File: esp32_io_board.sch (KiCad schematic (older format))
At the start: 58 parts, among them J1 USB_B_Micro, J11 Conn_01x02, J12 Conn_01x02, J13 Conn_01x02, J14 Conn_01x02, J2 Conn_02x04_Counter_Clockwise, J3 Conn_01x02, J4 Conn_01x04, J5 RASPBERRYPI-40-PIN-GPIO, J7 Conn_01x02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

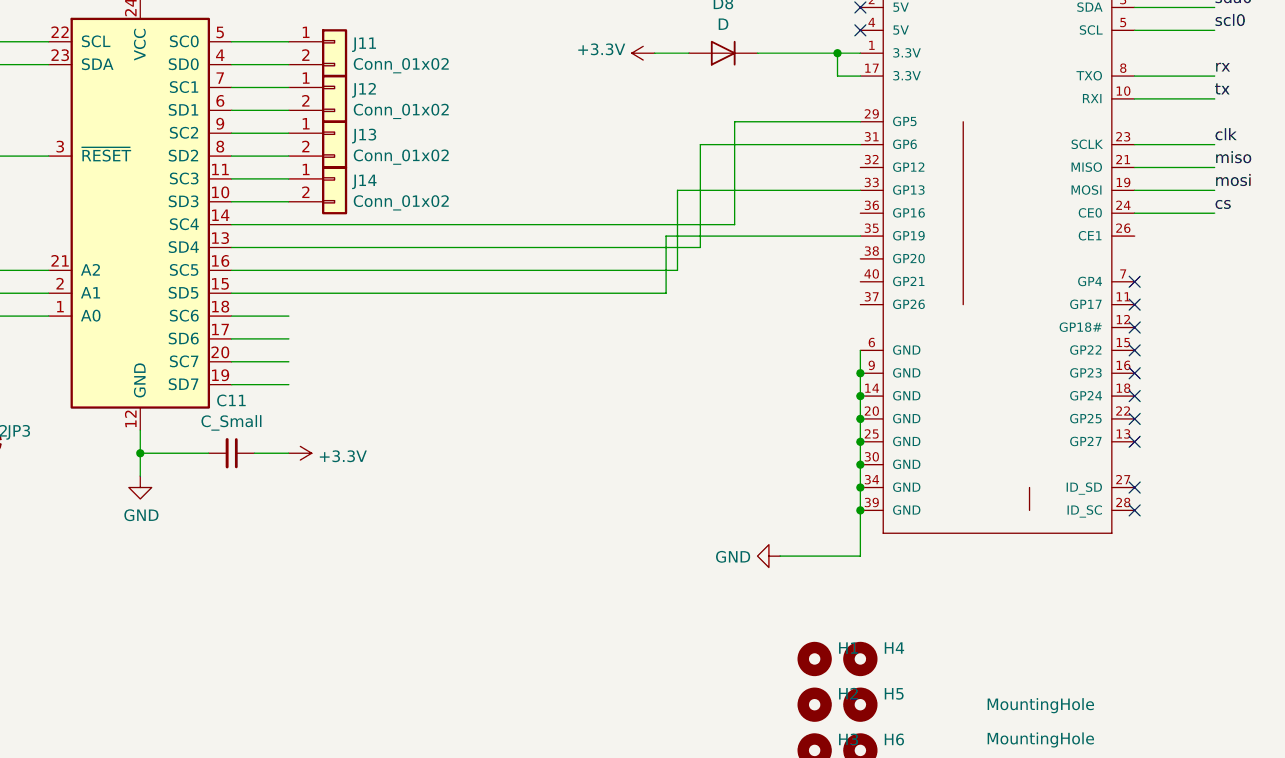
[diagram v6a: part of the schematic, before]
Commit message: raspberry pi integration
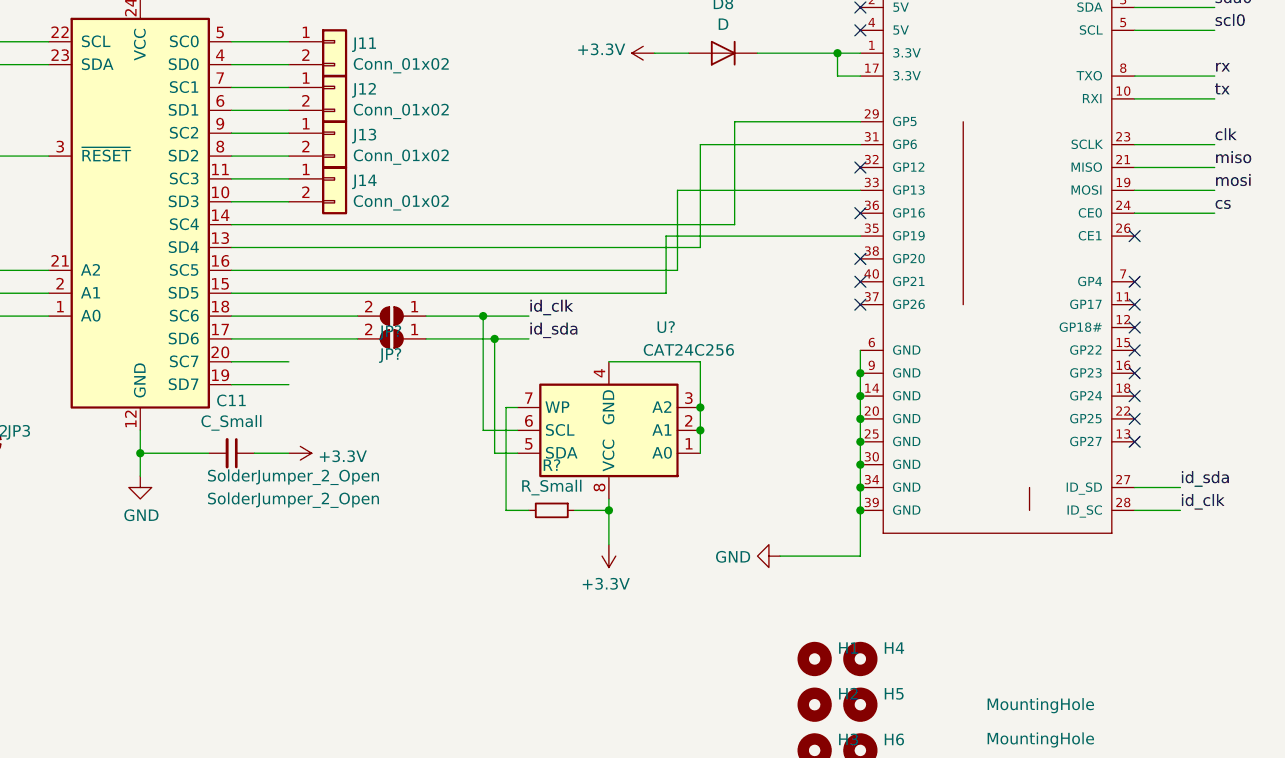
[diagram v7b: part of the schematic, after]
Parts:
- added JP? (x2): SolderJumper_2_Open, Jumper:SolderJumper-2_P1.3mm_Open_RoundedPad1.0x1.5mm, symbol Jumper:SolderJumper_2_Open
- added R?: R_Small, symbol Device:R_Small
- added U?: CAT24C256, symbol Memory_EEPROM:CAT24C256
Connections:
- net +3V3: now also R?.1, U?.8 (VCC)
- net id_sda: now reaches J5.27 (ID_SD)
- net id_sda: now also JP?.1 (A), U?.5 (SDA)
- net id_clk: now reaches J5.28 (ID_SC)
- net id_clk: now also JP?.1 (A), U?.6 (SCL)
- net at U6.17 (SD6): now also JP?.2 (B)
- net at U6.18 (SC6): now also JP?.2 (B)
- new net: U?.1 (A0), U?.2 (A1), U?.3 (A2), U?.4 (GND)
- new net: R?.2, U?.7 (WP)
- no-connect marks 30 -> 34
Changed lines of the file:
@@
 	12300 8450 12550 8450
-Wire Wire Line
-	12300 8950 12550 8950
-Wire Wire Line
-	12300 9050 12550 9050
 Wire Wire Line
 	12300 9150 12550 9150
@@
 NoConn ~ 16250 9400
 NoConn ~ 16250 9500
-NoConn ~ 16250 9700
-NoConn ~ 16250 9800
 NoConn ~ 9950 6950
 NoConn ~ 10250 6950
@@
 Wire Wire Line
 	14200 8600 14200 8850
+$Comp
+L Memory_EEPROM:CAT24C256 U?
+U 1 1 5C224C63
+P 13950 9450
+F 0 "U?" H 13700 9000 50  0000 C CNN
+F 1 "CAT24C256" H 13600 9100 50  0000 C CNN
+F 2 "" H 13950 9450 50  0001 C CNN
+F 3 "https://www.onsemi.cn/PowerSolutions/document/CAT24C256-D.PDF" H 13950 9450 50  0001 C CNN
+	1    13950 9450
+	-1   0    0    1
+$EndComp
+Wire Wire Line
+	13550 9450 13400 9450
+Wire Wire Line
+	13400 9450 13400 8950
+Wire Wire Line
+	12300 8950 12850 8950
+Wire Wire Line
+	13450 9050 13450 9550
+Wire Wire Line
+	13450 9550 13550 9550
+Wire Wire Line
+	12300 9050 12850 9050
+Wire Wire Line
+	14350 9550 14350 9450
+Wire Wire Line
+	14350 9150 13950 9150
+Connection ~ 14350 9350
+Wire Wire Line
+	14350 9350 14350 9150
+Connection ~ 14350 9450
+Wire Wire Line
+	14350 9450 14350 9350
+Wire Wire Line
+	13950 9750 13950 9800
+$Comp
+L power:+3.3V #PWR?
+U 1 1 5C2F17EF
+P 13950 9950
+F 0 "#PWR?" H 13950 9800 50  0001 C CNN
+F 1 "+3.3V" H 13965 10123 50  0000 C CNN
+F 2 "" H 13950 9950 50  0001 C CNN
+F 3 "" H 13950 9950 50  0001 C CNN
+	1    13950 9950
+	-1   0    0    1
+$EndComp
+Connection ~ 13450 9050
+Wire Wire Line
+	13400 8950 13600 8950
+Connection ~ 13400 8950
+Wire Wire Line
+	13450 9050 13600 9050
+Text Label 13600 8950 0    50   ~ 0
+id_clk
+Text Label 13600 9050 0    50   ~ 0
+id_sda
+Wire Wire Line
+	16250 9700 16450 9700
+Wire Wire Line
+	16250 9800 16450 9800
+Text Label 16450 9800 0    50   ~ 0
+id_clk
+Text Label 16450 9700 0    50   ~ 0
+id_sda
+$Comp
+L Jumper:SolderJumper_2_Open JP?
+U 1 1 5C387087
+P 13000 8950
+F 0 "JP?" H 12954 9018 50  0000 L CNN
+F 1 "SolderJumper_2_Open" H 13050 9650 50  0000 L CNN
+F 2 "Jumper:SolderJumper-2_P1.3mm_Open_RoundedPad1.0x1.5mm" H 13000 8950 50  0001 C CNN
+F 3 "~" H 13000 8950 50  0001 C CNN
+	1    13000 8950
+	-1   0    0    1
+$EndComp
+Wire Wire Line
+	13150 8950 13400 8950
+Wire Wire Line
+	13150 9050 13450 9050
+$Comp
+L Jumper:SolderJumper_2_Open JP?
+U 1 1 5C3A9876
+P 13000 9050
+F 0 "JP?" H 12954 9118 50  0000 L CNN
+F 1 "SolderJumper_2_Open" H 13050 9750 50  0000 L CNN
+F 2 "Jumper:SolderJumper-2_P1.3mm_Open_RoundedPad1.0x1.5mm" H 13000 9050 50  0001 C CNN
+F 3 "~" H 13000 9050 50  0001 C CNN
+	1    13000 9050
+	-1   0    0    1
+$EndComp
+NoConn ~ 15050 8300
+NoConn ~ 15050 8500
+NoConn ~ 15050 8700
+NoConn ~ 15050 8800
+NoConn ~ 15050 8900
+NoConn ~ 16250 8600
+Wire Wire Line
+	13550 9350 13500 9350
+Wire Wire Line
+	13500 9350 13500 9800
+$Comp
+L Device:R_Small R?
+U 1 1 5C4EC3FB
+P 13700 9800
+F 0 "R?" V 13504 9800 50  0000 C CNN
+F 1 "R_Small" V 13595 9800 50  0000 C CNN
+F 2 "" H 13700 9800 50  0001 C CNN
+F 3 "~" H 13700 9800 50  0001 C CNN
+	1    13700 9800
+	0    1    1    0
+$EndComp
+Wire Wire Line
+	13500 9800 13600 9800
+Wire Wire Line
+	13800 9800 13950 9800
+Connection ~ 13950 9800
+Wire Wire Line
+	13950 9800 13950 9950
 $EndSCHEMATC

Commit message: i2c jumpers
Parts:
- added JP? (x4): SolderJumper_2_Open, Jumper:SolderJumper-2_P1.3mm_Open_RoundedPad1.0x1.5mm, symbol Jumper:SolderJumper_2_Open
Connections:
- net at J5.29 (GP5): now also JP?.1 (A); no longer U6.14 (SC4)
- net at J5.31 (GP6): now also JP?.1 (A); no longer U6.13 (SD4)
- net at J5.33 (GP13): now also JP?.1 (A); no longer U6.16 (SC5)
- net at J5.35 (GP19): now also JP?.1 (A); no longer U6.15 (SD5)
- new net: JP?.2 (B), U6.15 (SD5)
- new net: JP?.2 (B), U6.16 (SC5)
- new net: JP?.2 (B), U6.13 (SD4)
- new net: JP?.2 (B), U6.14 (SC4)
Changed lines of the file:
@@
 	14500 8100 15050 8100
 Wire Wire Line
-	12300 8550 14500 8550
+	12300 8550 12850 8550
 Wire Wire Line
 	14350 8650 14350 8200
@@
 	14350 8200 15050 8200
 Wire Wire Line
-	12300 8650 14350 8650
+	12300 8650 12850 8650
 Wire Wire Line
 	14250 8750 14250 8400
 Wire Wire Line
-	12300 8750 14250 8750
+	12300 8750 12850 8750
 Wire Wire Line
 	14250 8400 15050 8400
 Wire Wire Line
-	12300 8850 14200 8850
+	12300 8850 12850 8850
 Wire Wire Line
 	14200 8600 15050 8600
@@
 P 13000 8950
 F 0 "JP?" H 12954 9018 50  0000 L CNN
-F 1 "SolderJumper_2_Open" H 13050 9650 50  0000 L CNN
+F 1 "SolderJumper_2_Open" H 12950 10000 50  0000 L CNN
 F 2 "Jumper:SolderJumper-2_P1.3mm_Open_RoundedPad1.0x1.5mm" H 13000 8950 50  0001 C CNN
 F 3 "~" H 13000 8950 50  0001 C CNN
@@
 P 13000 9050
 F 0 "JP?" H 12954 9118 50  0000 L CNN
-F 1 "SolderJumper_2_Open" H 13050 9750 50  0000 L CNN
+F 1 "SolderJumper_2_Open" H 12950 10100 50  0000 L CNN
 F 2 "Jumper:SolderJumper-2_P1.3mm_Open_RoundedPad1.0x1.5mm" H 13000 9050 50  0001 C CNN
 F 3 "~" H 13000 9050 50  0001 C CNN
@@
 Wire Wire Line
 	13950 9800 13950 9950
+Wire Wire Line
+	13150 8850 14200 8850
+Wire Wire Line
+	13150 8750 14250 8750
+Wire Wire Line
+	13150 8650 14350 8650
+Wire Wire Line
+	13150 8550 14500 8550
+$Comp
+L Jumper:SolderJumper_2_Open JP?
+U 1 1 5C239362
+P 13000 8850
+F 0 "JP?" H 12954 8918 50  0000 L CNN
+F 1 "SolderJumper_2_Open" H 12950 10200 50  0000 L CNN
+F 2 "Jumper:SolderJumper-2_P1.3mm_Open_RoundedPad1.0x1.5mm" H 13000 8850 50  0001 C CNN
+F 3 "~" H 13000 8850 50  0001 C CNN
+	1    13000 8850
+	-1   0    0    1
+$EndComp
+$Comp
+L Jumper:SolderJumper_2_Open JP?
+U 1 1 5C2397B0
+P 13000 8750
+F 0 "JP?" H 12954 8818 50  0000 L CNN
+F 1 "SolderJumper_2_Open" H 12950 10500 50  0000 L CNN
+F 2 "Jumper:SolderJumper-2_P1.3mm_Open_RoundedPad1.0x1.5mm" H 13000 8750 50  0001 C CNN
+F 3 "~" H 13000 8750 50  0001 C CNN
+	1    13000 8750
+	-1   0    0    1
+$EndComp
+$Comp
+L Jumper:SolderJumper_2_Open JP?
+U 1 1 5C239840
+P 13000 8650
+F 0 "JP?" H 12954 8718 50  0000 L CNN
+F 1 "SolderJumper_2_Open" H 12950 10400 50  0000 L CNN
+F 2 "Jumper:SolderJumper-2_P1.3mm_Open_RoundedPad1.0x1.5mm" H 13000 8650 50  0001 C CNN
+F 3 "~" H 13000 8650 50  0001 C CNN
+	1    13000 8650
+	-1   0    0    1
+$EndComp
+$Comp
+L Jumper:SolderJumper_2_Open JP?
+U 1 1 5C239B5B
+P 13000 8550
+F 0 "JP?" H 12954 8618 50  0000 L CNN
+F 1 "SolderJumper_2_Open" H 12950 10300 50  0000 L CNN
+F 2 "Jumper:SolderJumper-2_P1.3mm_Open_RoundedPad1.0x1.5mm" H 13000 8550 50  0001 C CNN
+F 3 "~" H 13000 8550 50  0001 C CNN
+	1    13000 8550
+	-1   0    0    1
+$EndComp
 $EndSCHEMATC
